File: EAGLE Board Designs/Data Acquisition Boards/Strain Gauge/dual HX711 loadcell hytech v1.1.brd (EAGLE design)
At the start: 114.3 x 44.1 mm, 48 parts, among them Q1 MMBT4403, Q2 MMBT4403, U1 HX711, U2 HX711, X1 CONNECTOR-6, X2 CONNECTOR-2, X4 CONNECTOR-4, X5 CONNECTOR-4

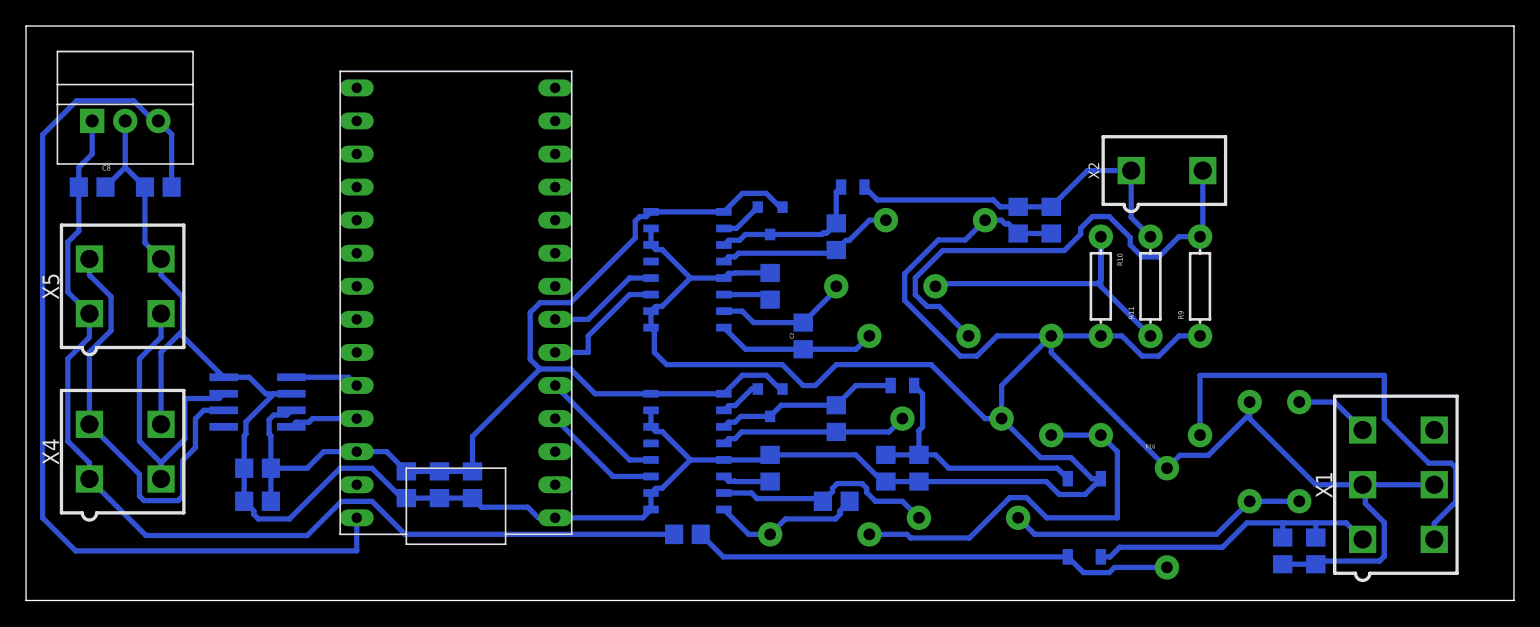
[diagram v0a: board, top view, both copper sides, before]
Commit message: v1.1 is designed to use GTMS load cells
GTMS load cells can be excited by the 3.3V output of the HX711 so no complication is neeeded regarding voltage dividers or an optocoupler
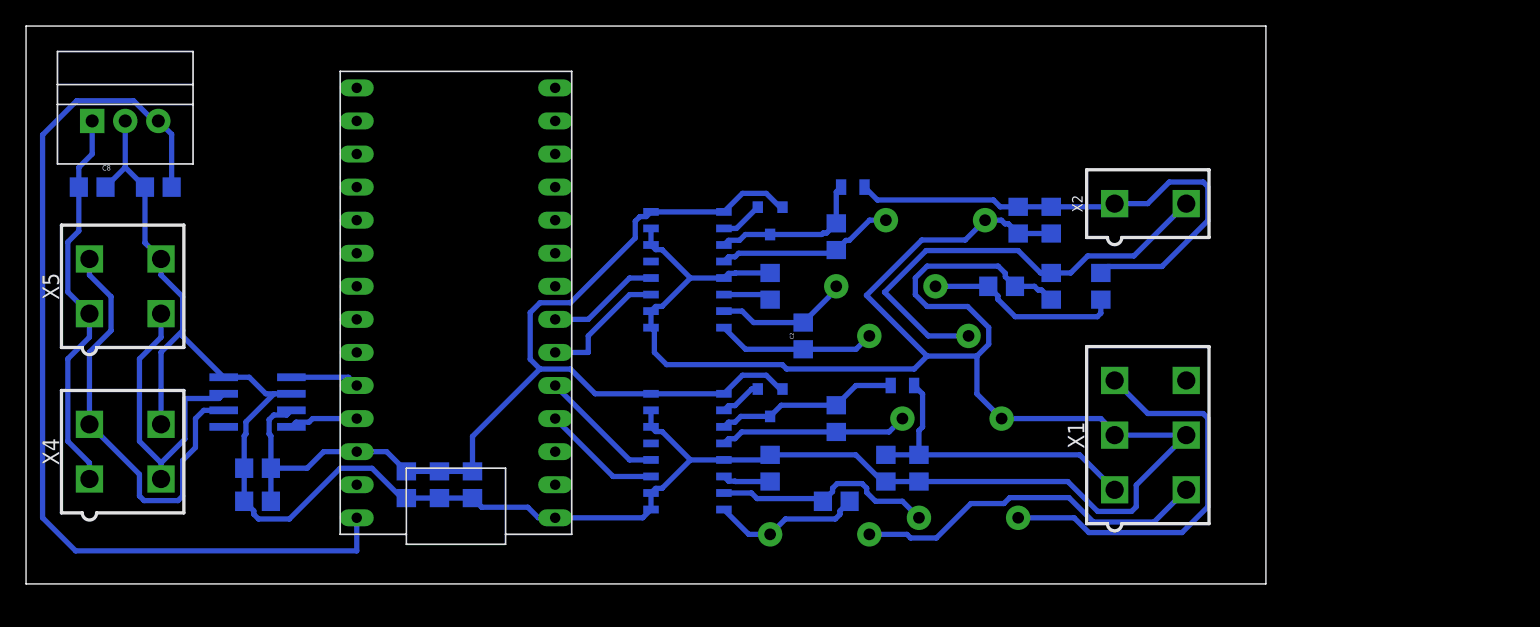
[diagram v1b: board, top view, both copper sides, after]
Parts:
- removed C13: 1uF, HyTechDevices:0805
- removed C14: .1uF, HyTechDevices:0805
- removed R16, R7: 6800, HyTechDevices:AXIAL-0.3
- removed R17, R8: 3300, HyTechDevices:AXIAL-0.3
- removed R5: 200, HyTechDevices:0805
- removed R6: 1000, HyTechDevices:AXIAL-0.3
- removed U$2: CPC1002N, HyTechDevices:SOP04
- R10, R11, R9: device HyTechDevices:AXIAL-0.3 -> HyTechDevices:0805
- moved X1 19.4 mm to (96.5, 12.7)
- moved R9 11.4 mm to (88.9, 24.1), flipped to the bottom
- moved R10 7.62 mm to (85.1, 24.1), flipped to the bottom, turned to 180 degrees
- moved R11 3.81 mm to (92.7, 24.1), flipped to the bottom
- moved X2 2.84 mm to (96.5, 30.5)
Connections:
- removed net N$13: R16.P$2, X1.4
- removed net N$14: C13.2, C14.2, U$2.3, X1.1
- removed net N$15: R5.2, R6.P$1, U$2.4
- removed net N$16: R7.P$2, X1.3
- net A+: now also X1.4; no longer R16.P$1, R17.P$2
- net A+2: now also R9.2; no longer R9.P$2
- net A-: now also X1.3; no longer R7.P$1, R8.P$2
- net A-2: now also R10.1, R11.1; no longer R10.P$1, R11.P$1
- net AVDD: now also X1.1; no longer U$2.1
- net AVDD2: now also R11.2; no longer R11.P$2
- net GND: now also R10.2, R9.1; no longer C13.1, C14.1, R10.P$2, R17.P$1, R6.P$2, R8.P$1, R9.P$1, U$2.2
- net VIN: no longer R5.1
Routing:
- net VIN: track 79.2 -> 30.3 mm
- net GND: track 290.3 -> 248.7 mm
- net N$15: track 37.2 -> 0.00 mm
- net N$13: track 35.3 -> 0.00 mm
- net N$14: track 24.0 -> 0.00 mm
- net AVDD2: track 28.0 -> 40.4 mm
- net A-2: track 25.4 -> 15.0 mm
- net A-: track 23.2 -> 31.0 mm
- net N$16: track 5.76 -> 0.00 mm
- net A+: track 31.8 -> 27.5 mm
- net AVDD: track 20.4 -> 24.4 mm
- net A+2: track 38.2 -> 35.3 mm
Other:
- board size 114.3 x 44.1 mm -> 95.2 x 42.8 mm
